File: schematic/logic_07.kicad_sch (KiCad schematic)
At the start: 1 part, among them U424 74HC32

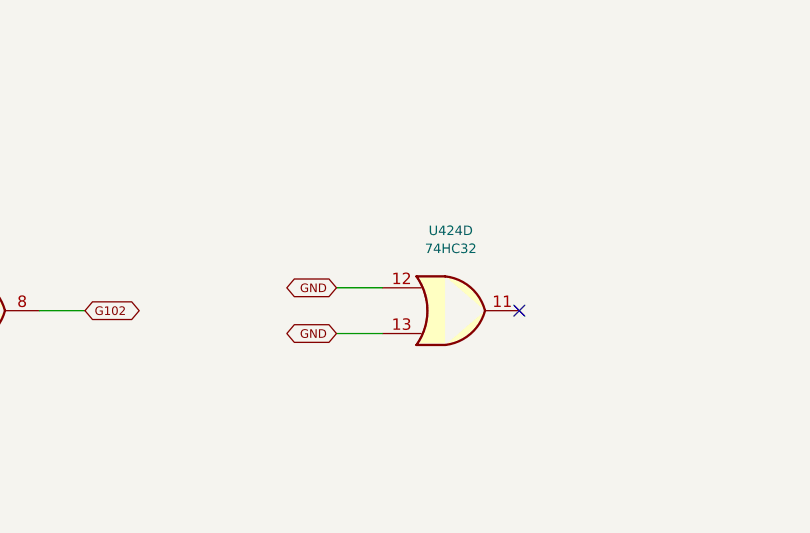
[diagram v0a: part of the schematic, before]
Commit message: add power supply, rail checks and parts list
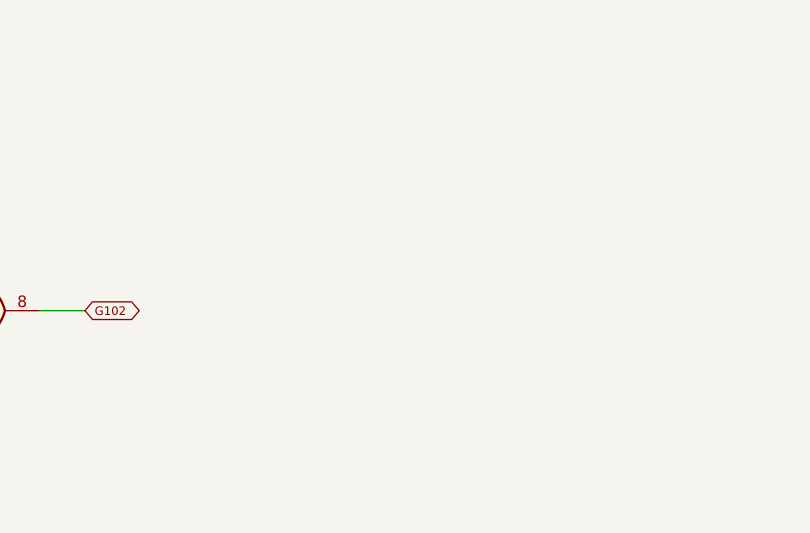
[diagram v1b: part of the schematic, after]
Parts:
- removed unit 4 of U424
- U424: MPN (none) -> 74HC32D,653; Manufacturer (none) -> Nexperia; Supplier (none) -> LCSC
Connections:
- no-connect marks 1 -> 0
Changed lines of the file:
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@@
       )
     )
-    (property "Datasheet" "http://www.ti.com/lit/gpn/sn74LS32"
+    (property "Datasheet" "https://assets.nexperia.com/documents/data-sheet/74HC_HCT32.pdf"
       (at 39.37 40.64 0.0)
       (effects
         (font
           (size 1.05 1.05)
+        )
+        (hide yes)
+      )
+    )
+    (property "MPN" "74HC32D,653"
+      (at 39.37 49.53 0.0)
+      (effects
+        (font
+          (size 1.0 1.0)
+        )
+        (hide yes)
+      )
+    )
+    (property "Manufacturer" "Nexperia"
+      (at 39.37 49.53 0.0)
+      (effects
+        (font
+          (size 1.0 1.0)
+        )
+        (hide yes)
+      )
+    )
+    (property "Supplier" "LCSC"
+      (at 39.37 49.53 0.0)
+      (effects
+        (font
+          (size 1.0 1.0)
         )
         (hide yes)
@@
       )
     )
-    (property "Datasheet" "http://www.ti.com/lit/gpn/sn74LS32"
+    (property "Datasheet" "https://assets.nexperia.com/documents/data-sheet/74HC_HCT32.pdf"
       (at 93.98 40.64 0.0)
       (effects
         (font
           (size 1.05 1.05)
+        )
+        (hide yes)
+      )
+    )
+    (property "MPN" "74HC32D,653"
+      (at 93.98 49.53 0.0)
+      (effects
+        (font
+          (size 1.0 1.0)
+        )
+        (hide yes)
+      )
+    )
+    (property "Manufacturer" "Nexperia"
+      (at 93.98 49.53 0.0)
+      (effects
+        (font
+          (size 1.0 1.0)
+        )
+        (hide yes)
+      )
+    )
+    (property "Supplier" "LCSC"
+      (at 93.98 49.53 0.0)
+      (effects
+        (font
+          (size 1.0 1.0)
         )
         (hide yes)
@@
       )
     )
-    (property "Datasheet" "http://www.ti.com/lit/gpn/sn74LS32"
+    (property "Datasheet" "https://assets.nexperia.com/documents/data-sheet/74HC_HCT32.pdf"
       (at 148.59 40.64 0.0)
       (effects
         (font
           (size 1.05 1.05)
+        )
+        (hide yes)
+      )
+    )
+    (property "MPN" "74HC32D,653"
+      (at 148.59 49.53 0.0)
+      (effects
+        (font
+          (size 1.0 1.0)
+        )
+        (hide yes)
+      )
+    )
+    (property "Manufacturer" "Nexperia"
+      (at 148.59 49.53 0.0)
+      (effects
+        (font
+          (size 1.0 1.0)
+        )
+        (hide yes)
+      )
+    )
+    (property "Supplier" "LCSC"
+      (at 148.59 49.53 0.0)
+      (effects
+        (font
+          (size 1.0 1.0)
         )
         (hide yes)
@@
     (shape bidirectional)
     (at 135.89 52.07 180.0)
-    (effects
-      (font
-        (size 0.95 0.95)
-      )
-      (justify right)
-    )
-  )
-  (symbol
-    (lib_id "74xx:74LS32")
-    (at 201.93 49.53 0.0)
-    (unit 4)
-    (exclude_from_sim no)
-    (in_bom yes)
-    (on_board yes)
-    (dnp no)
-    (property "Reference" "U424"
-      (at 201.93 40.64 0.0)
-      (effects
-        (font
-          (size 1.05 1.05)
-        )
-      )
-    )
-    (property "Value" "74HC32"
-      (at 201.93 42.64 0.0)
-      (effects
-        (font
-          (size 1.05 1.05)
-        )
-      )
-    )
-    (property "Footprint" "Package_SO:SOIC-14_3.9x8.7mm_P1.27mm"
-      (at 201.93 40.64 0.0)
-      (effects
-        (font
-          (size 1.05 1.05)
-        )
-        (hide yes)
-      )
-    )
-    (property "Datasheet" "http://www.ti.com/lit/gpn/sn74LS32"
-      (at 201.93 40.64 0.0)
-      (effects
-        (font
-          (size 1.05 1.05)
-        )
-        (hide yes)
-      )
-    )
-    (instances
-      (project "arpeggiator"
-        (path "/b74f2899-8338-4c76-a1a7-8fd841787321/c79f4253-7072-5222-b1fa-f2c67fce914b"
-          (reference "U424")
-          (unit 4)
-        )
-      )
-    )
-  )
-  (no_connect
-    (at 209.55 49.53)
-  )
-  (wire
-    (pts
-      (xy 194.31 46.99)
-      (xy 189.23 46.99)
-    )
-    (stroke
-      (width 0)
-      (type default)
-    )
-  )
-  (global_label "GND"
-    (shape bidirectional)
-    (at 189.23 46.99 180.0)
-    (effects
-      (font
-        (size 0.95 0.95)
-      )
-      (justify right)
-    )
-  )
-  (wire
-    (pts
-      (xy 194.31 52.07)
-      (xy 189.23 52.07)
-    )
-    (stroke
-      (width 0)
-      (type default)
-    )
-  )
-  (global_label "GND"
-    (shape bidirectional)
-    (at 189.23 52.07 180.0)
     (effects
       (font
@@
       )
     )
-    (property "Datasheet" "http://www.ti.com/lit/gpn/sn74LS32"
+    (property "Datasheet" "https://assets.nexperia.com/documents/data-sheet/74HC_HCT32.pdf"
       (at 260.35 46.99 0.0)
       (effects
@@
         )
         (justify left)
+        (hide yes)
+      )
+    )
+    (property "MPN" "74HC32D,653"
+      (at 256.54 49.53 0.0)
+      (effects
+        (font
+          (size 1.0 1.0)
+        )
+        (hide yes)
+      )
+    )
+    (property "Manufacturer" "Nexperia"
+      (at 256.54 49.53 0.0)
+      (effects
+        (font
+          (size 1.0 1.0)
+        )
+        (hide yes)
+      )
+    )
+    (property "Supplier" "LCSC"
+      (at 256.54 49.53 0.0)
+      (effects
+        (font
+          (size 1.0 1.0)
+        )
         (hide yes)
       )
@@
     (on_board no)
     (dnp no)
-    (property "Reference" "#PWR14037"
+    (property "Reference" "#PWR14031"
       (at 256.54 67.31 0.0)
       (effects
@@
       (project "arpeggiator"
         (path "/b74f2899-8338-4c76-a1a7-8fd841787321/c79f4253-7072-5222-b1fa-f2c67fce914b"
-          (reference "#PWR14037")
+          (reference "#PWR14031")
           (unit 1)
         )
@@
     (on_board no)
     (dnp no)
-    (property "Reference" "#PWR14039"
+    (property "Reference" "#PWR14033"
       (at 256.54 31.75 0.0)
       (effects
@@
       (project "arpeggiator"
         (path "/b74f2899-8338-4c76-a1a7-8fd841787321/c79f4253-7072-5222-b1fa-f2c67fce914b"
-          (reference "#PWR14039")
+          (reference "#PWR14033")
           (unit 1)
         )
